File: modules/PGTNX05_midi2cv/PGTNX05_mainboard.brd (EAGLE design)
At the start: 111.8 x 77.5 mm, 179 parts, among them IC1 H11L1, IC2 LM2574N-5.0, IC3 40106N, IC4 H11L1

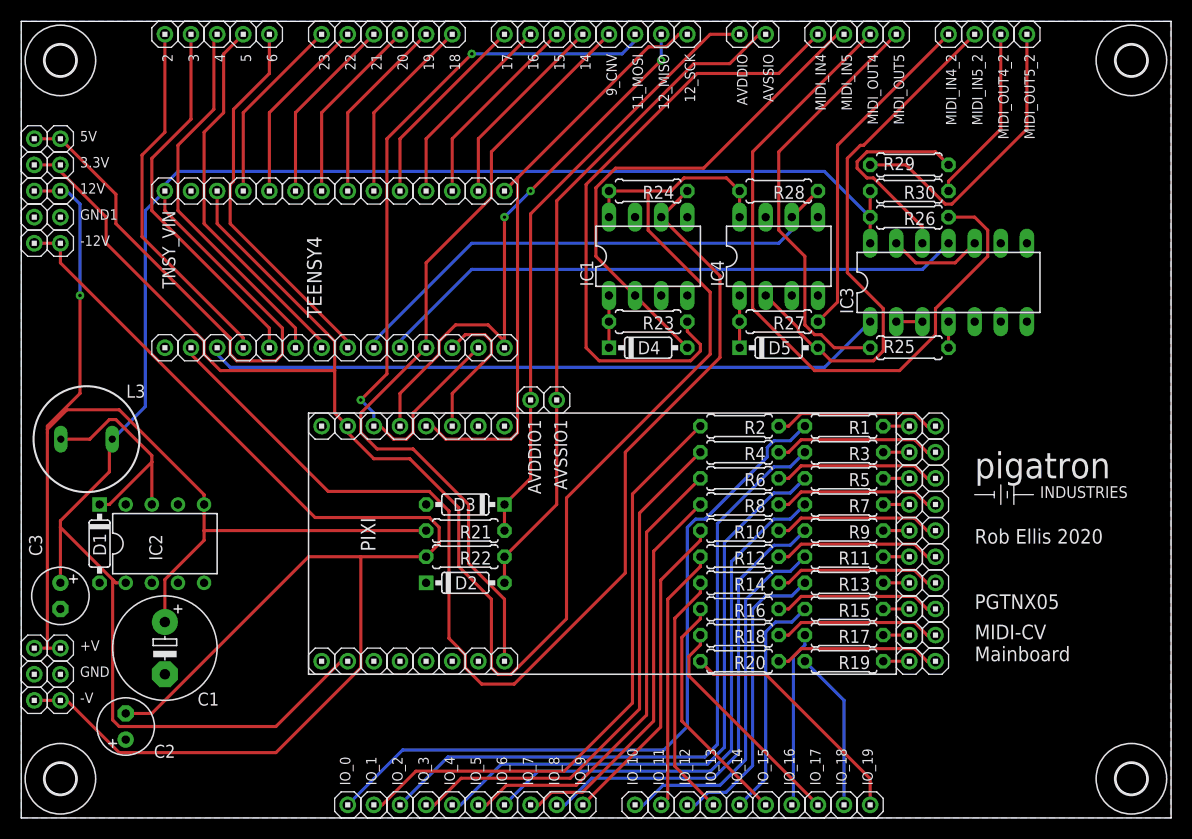
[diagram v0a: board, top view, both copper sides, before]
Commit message: Update PGTNX05_mainboard.brd
Tidied up dimensiosn docu, added extra mounting hole
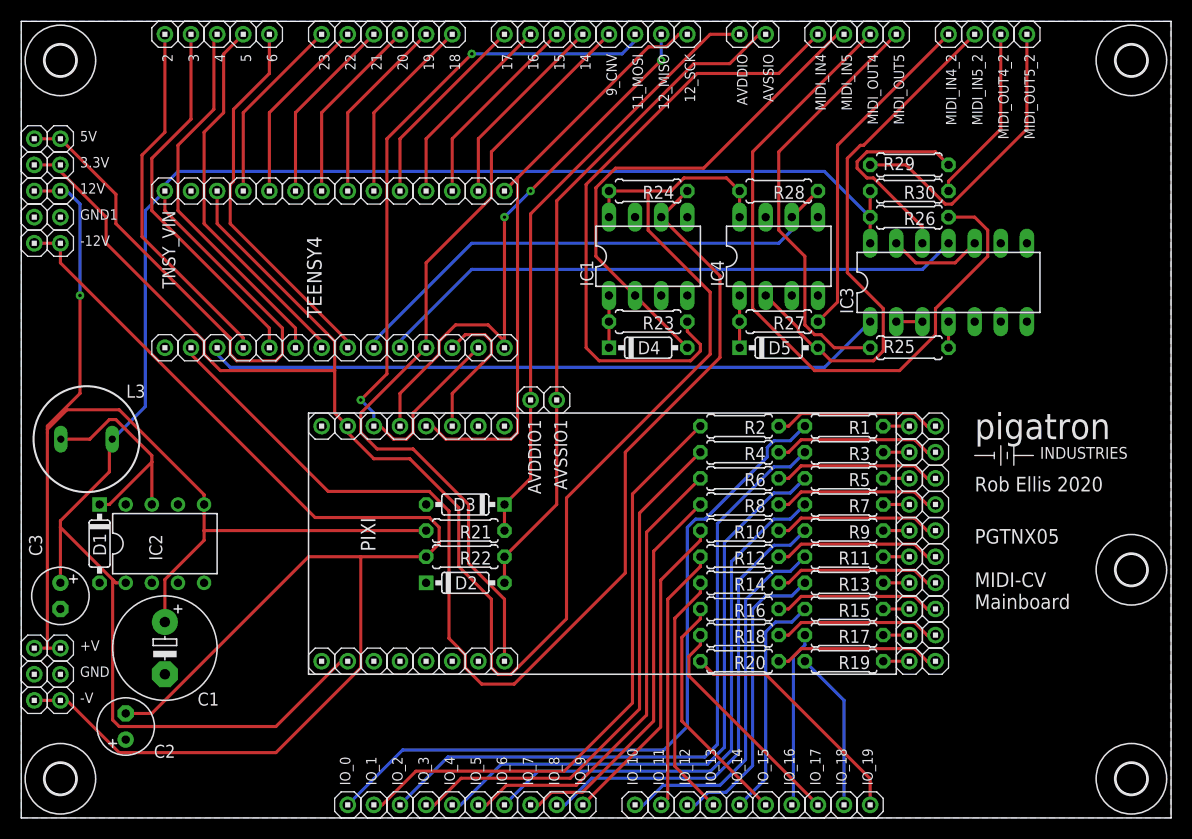
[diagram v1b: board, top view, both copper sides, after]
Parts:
- added U$1: (no value), mechanical:STANDOFF/3.0
- moved U$5 3.81 mm to (101.6, 36.8)
